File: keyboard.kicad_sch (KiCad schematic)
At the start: 69 parts, among them J1 USB_C_Receptacle_USB2.0_14P, Q1 NMOS, SW1 SW_Push, SW10 SW_Push, SW11 RotaryEncoder_Switch, SW2 SW_Push, SW3 SW_Push, SW4 SW_Push, SW5 SW_Push, SW6 SW_Push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

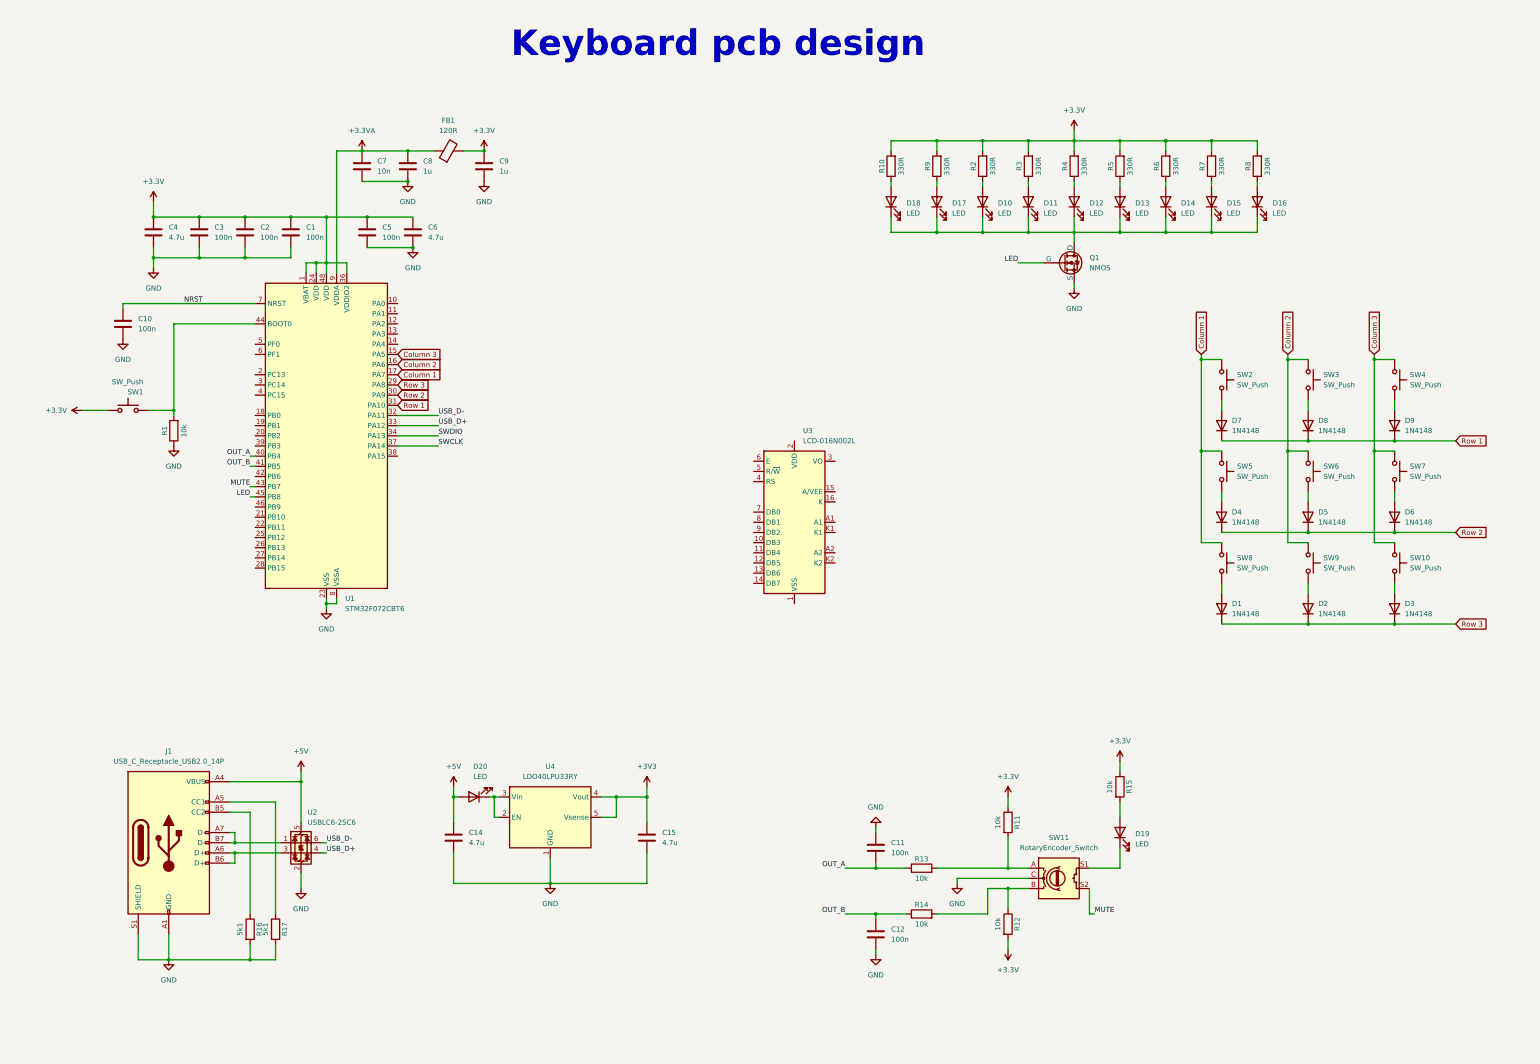
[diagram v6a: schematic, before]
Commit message: Added lcd display
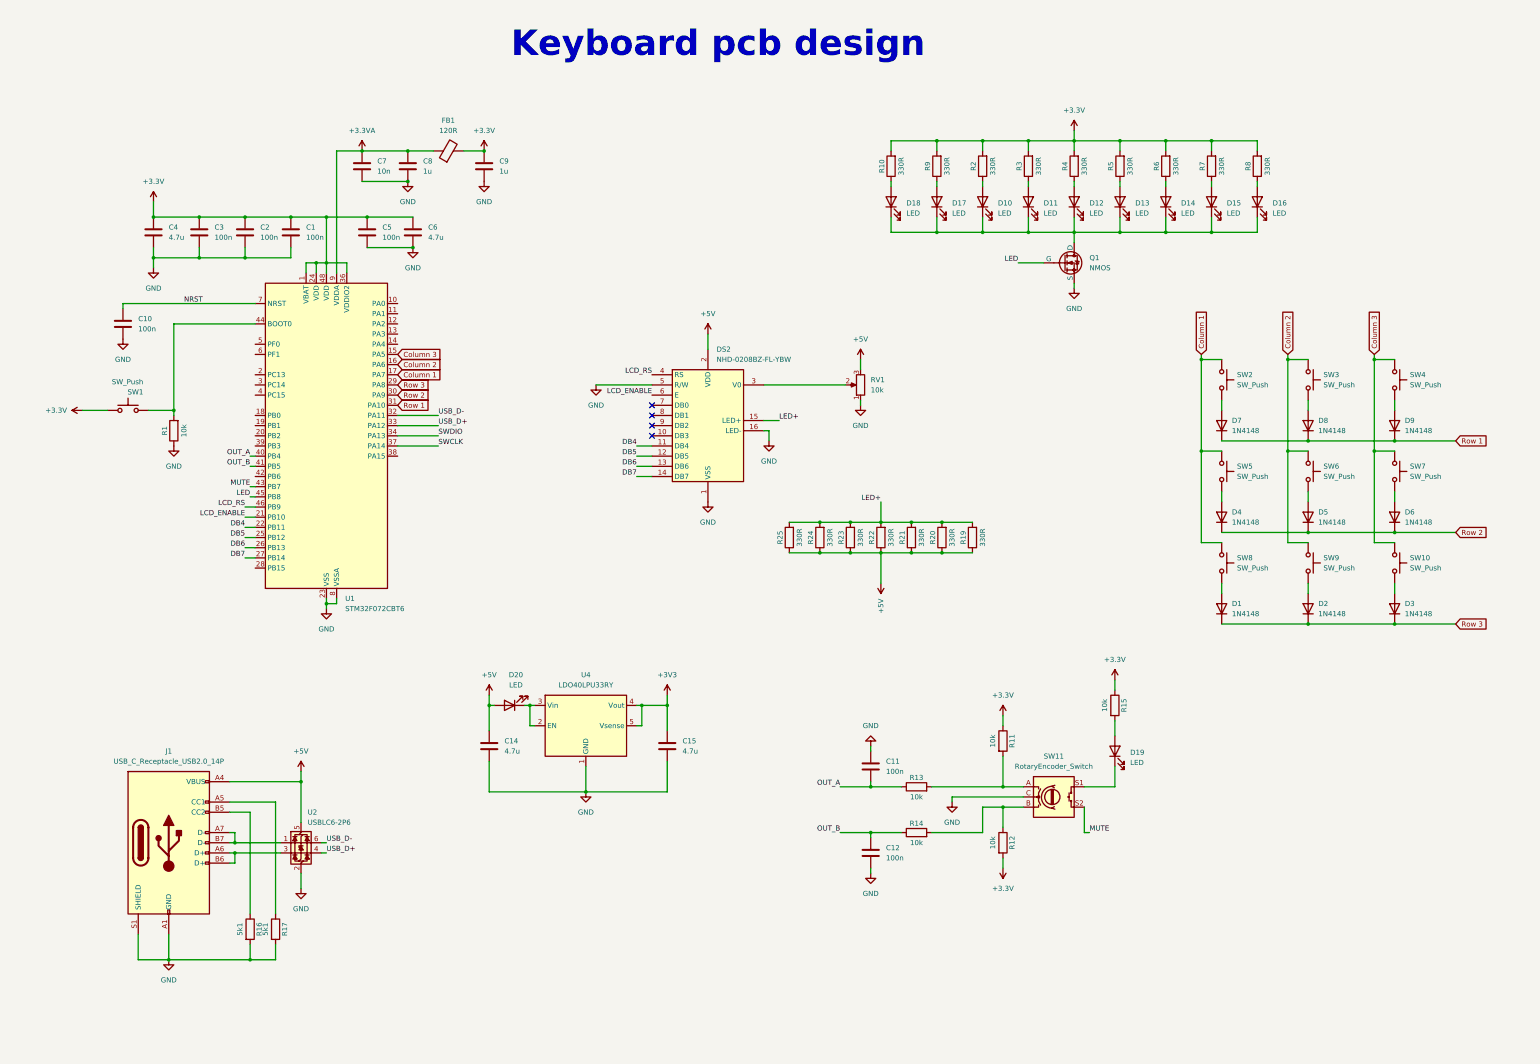
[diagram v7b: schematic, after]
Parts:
- removed U2: USBLC6-2SC6, Package_TO_SOT_SMD:SOT-23-6, symbol Power_Protection:USBLC6-2SC6
- removed U3: LCD-016N002L, Display:LCD-016N002L, symbol Display_Character:LCD-016N002L
- added DS2: NHD-0208BZ-FL-YBW, NHD0208BZFLYBW, symbol NHD-0208BZ-FL-YBW:NHD-0208BZ-FL-YBW
- added R19, R20, R21, R22, R23, R24, R25: 330R, symbol Device:R
- added RV1: 10k, symbol Device:R_Potentiometer
- added U2: USBLC6-2P6, Package_TO_SOT_SMD:SOT-666, symbol Power_Protection:USBLC6-2P6
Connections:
- net +5V: now also DS2.2 (VDD), R19.1, R20.1, R21.1, R22.1, R23.1, R24.1, R25.1, RV1.3, U2.5 (VBUS)
- net GND: now also DS2.1 (VSS), DS2.16 (LED-), DS2.5 (R/W), RV1.1, U2.2 (GND)
- net USB_D+: now also U2.4 (I/O2)
- net USB_D-: now also U2.6 (I/O1)
- net at J1.A7 (D-), J1.B7 (D-): now also U2.1 (I/O1)
- net at J1.A6 (D+), J1.B6 (D+): now also U2.3 (I/O2)
- net LCD_ENABLE: now reaches U1.21 (PB10)
- net LCD_ENABLE: now also DS2.6 (E)
- net DB4: now reaches U1.22 (PB11)
- net DB4: now also DS2.11 (DB4)
- net DB5: now reaches U1.25 (PB12)
- net DB5: now also DS2.12 (DB5)
- net DB6: now reaches U1.26 (PB13)
- net DB6: now also DS2.13 (DB6)
- net DB7: now reaches U1.27 (PB14)
- net DB7: now also DS2.14 (DB7)
- net LCD_RS: now reaches U1.46 (PB9)
- net LCD_RS: now also DS2.4 (RS)
- new net: DS2.3 (V0), RV1.2
- new net LED+: DS2.15 (LED+), R19.2, R20.2, R21.2, R22.2, R23.2, R24.2, R25.2
- no-connect marks 0 -> 4
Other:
- moved on the sheet: C11, C12, C14, C15, D19, D20, R11, R12, R13, R14, R15, SW11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

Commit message: Added key switches footprints
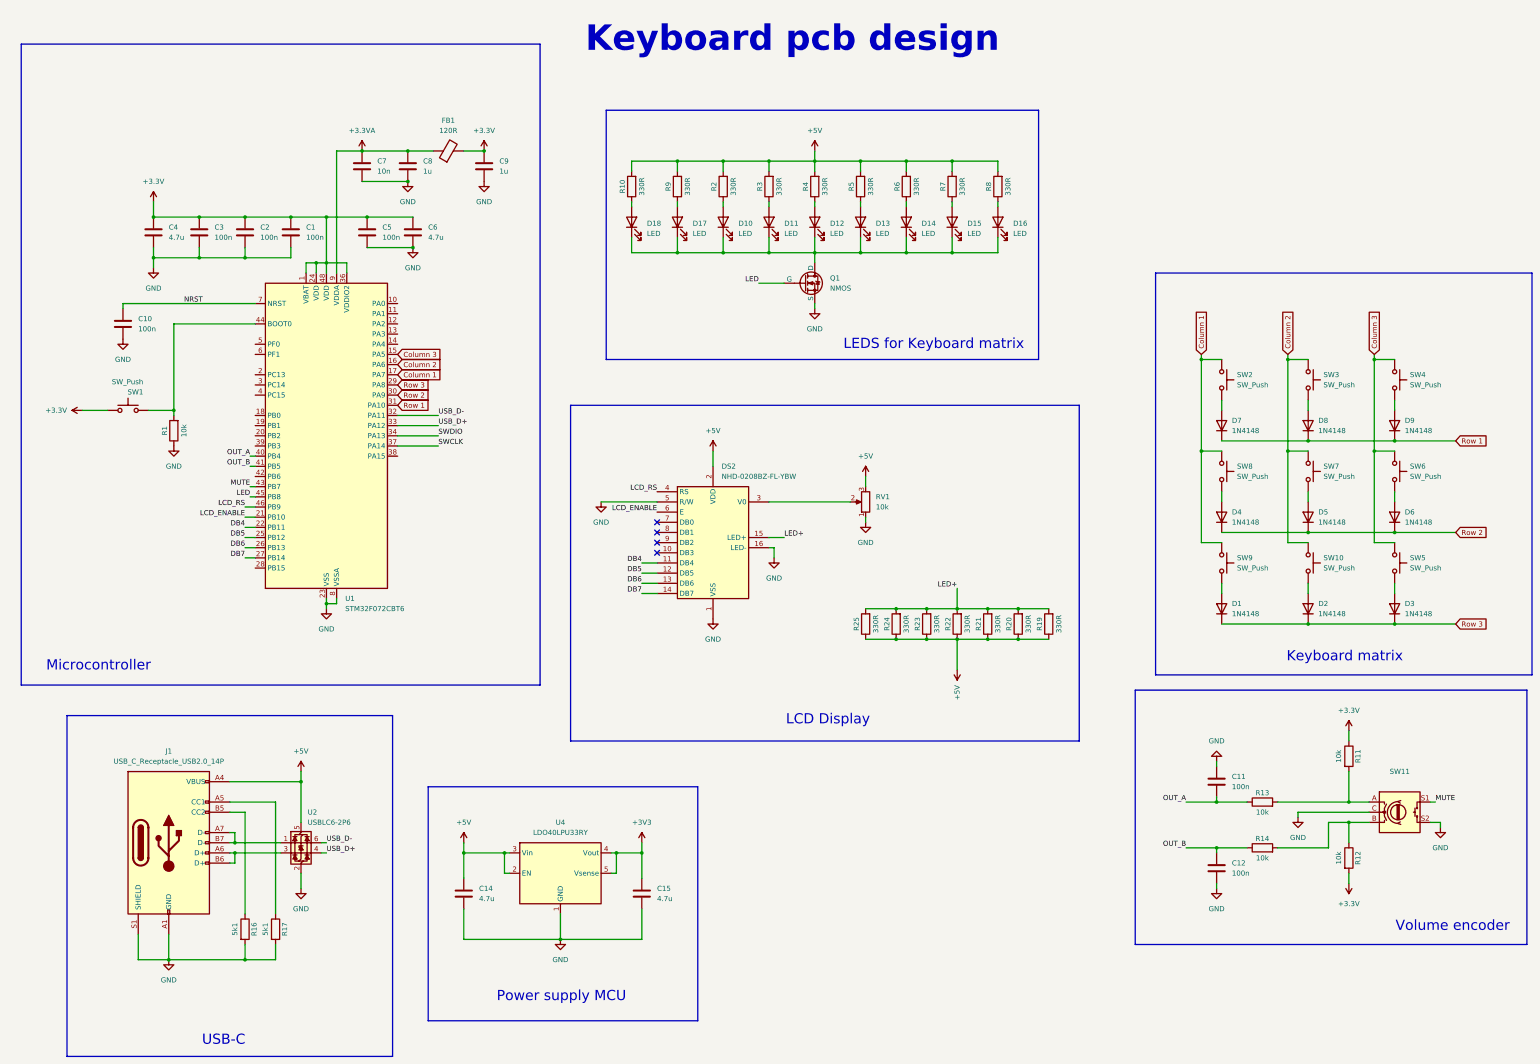
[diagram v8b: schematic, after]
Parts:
- removed D19, D20: LED, symbol Device:LED
- removed R15: 10k, symbol Device:R
- SW10, SW2, SW3, SW4, SW5, SW6, SW7, SW8, SW9: footprint (none) -> Switch_Keyboard_Cherry_MX:SW_Cherry_MX_PCB_1.00u
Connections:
- net +3.3V: no longer R10.2, R2.2, R3.2, R4.2, R5.2, R6.2, R7.2, R8.2, R9.2
- net +5V: now also R10.2, R2.2, R3.2, R4.2, R5.2, R6.2, R7.2, R8.2, R9.2, U4.2 (EN), U4.3 (Vin)
- net Column 1: now also SW9.1; no longer SW5.1
- net Column 2: now also SW10.1, SW7.1; no longer SW6.1, SW9.1
- net Column 3: now also SW5.1, SW6.1; no longer SW10.1, SW7.1
- net GND: now also SW11.S2
- net MUTE: now also SW11.S1; no longer SW11.S2
- net at D4.2 (A): now also SW8.2; no longer SW5.2
- net at D1.2 (A): now also SW9.2; no longer SW8.2
- net at D5.2 (A): now also SW7.2; no longer SW6.2
- net at D6.2 (A): now also SW6.2; no longer SW7.2
- net at D2.2 (A): now also SW10.2; no longer SW9.2
- net at D3.2 (A): now also SW5.2; no longer SW10.2
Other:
- note added: "Keyboard matrix"
- note added: "LCD Display"
- note added: "LEDS for Keyboard matrix"
- note added: "Microcontroller"
- note added: "Power supply MCU"
- note added: "USB-C"
- note added: "Volume encoder"
- moved on the sheet: C11, C12, C14, C15, D10, D11, D12, D13, D14, D15, D16, D17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
